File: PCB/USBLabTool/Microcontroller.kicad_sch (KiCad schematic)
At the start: 18 parts, among them J1 Conn_01x06_Pin, J18 02x02, J21 Conn_01x20_Pin, SW2 PTH_RA_h7.5mm, U12 STM32H562VGTx, Y1 32.768kHz

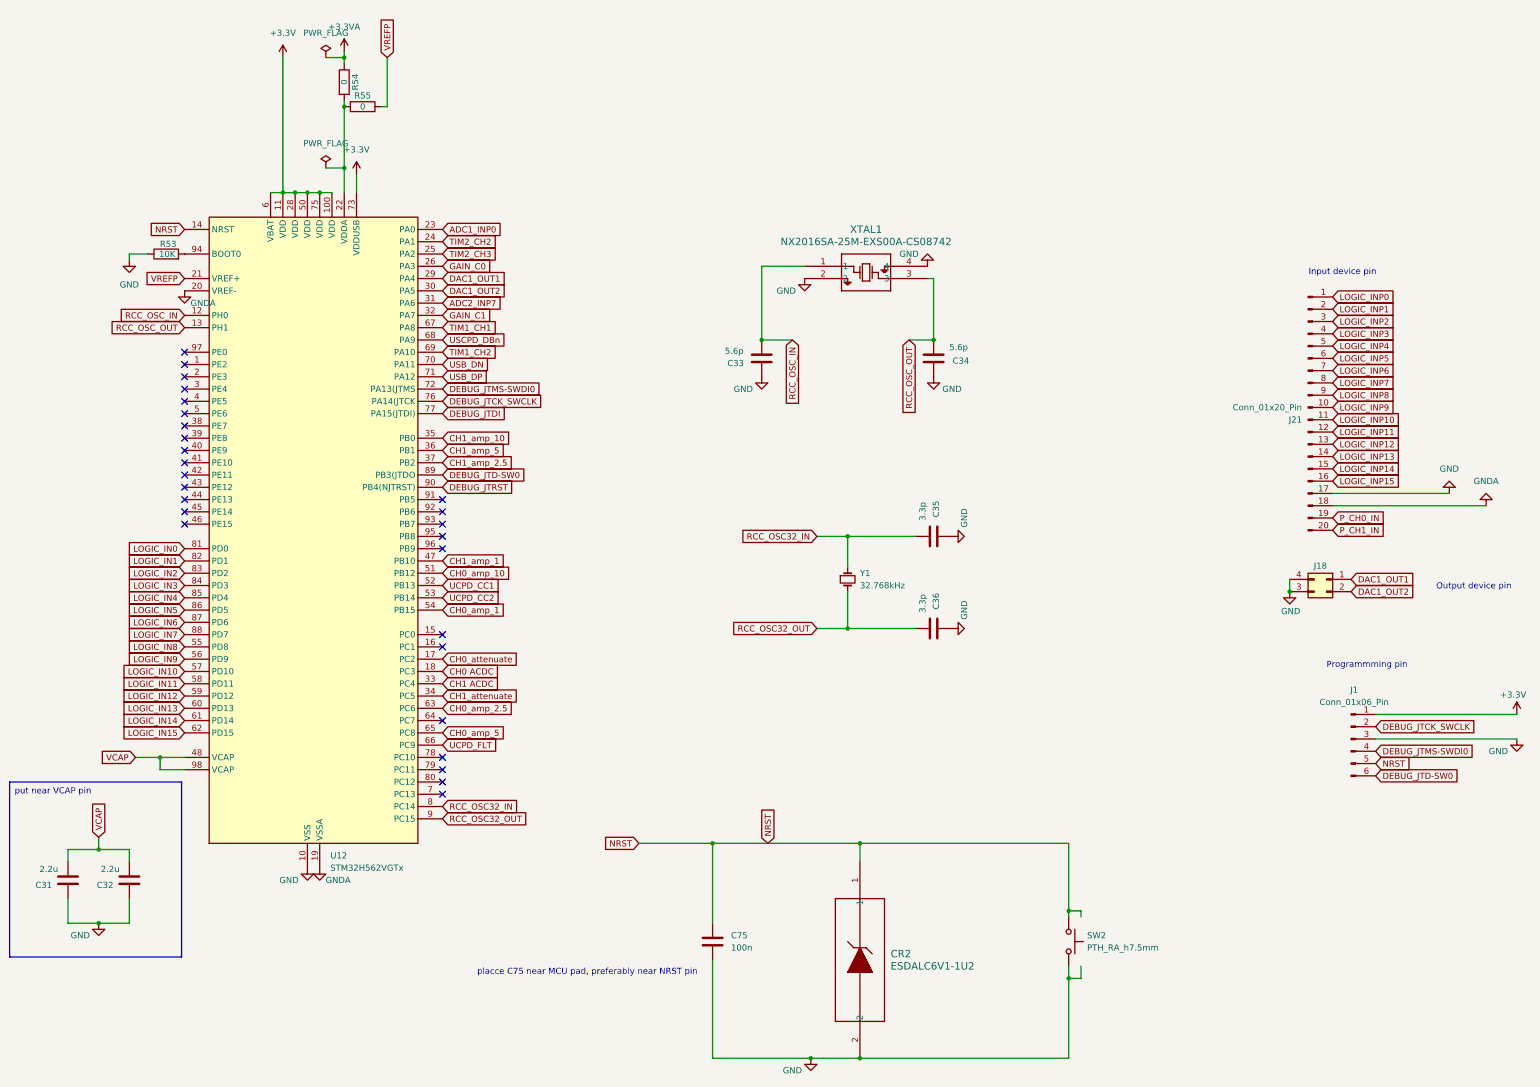
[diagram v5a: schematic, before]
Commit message: footprint with minor fixes
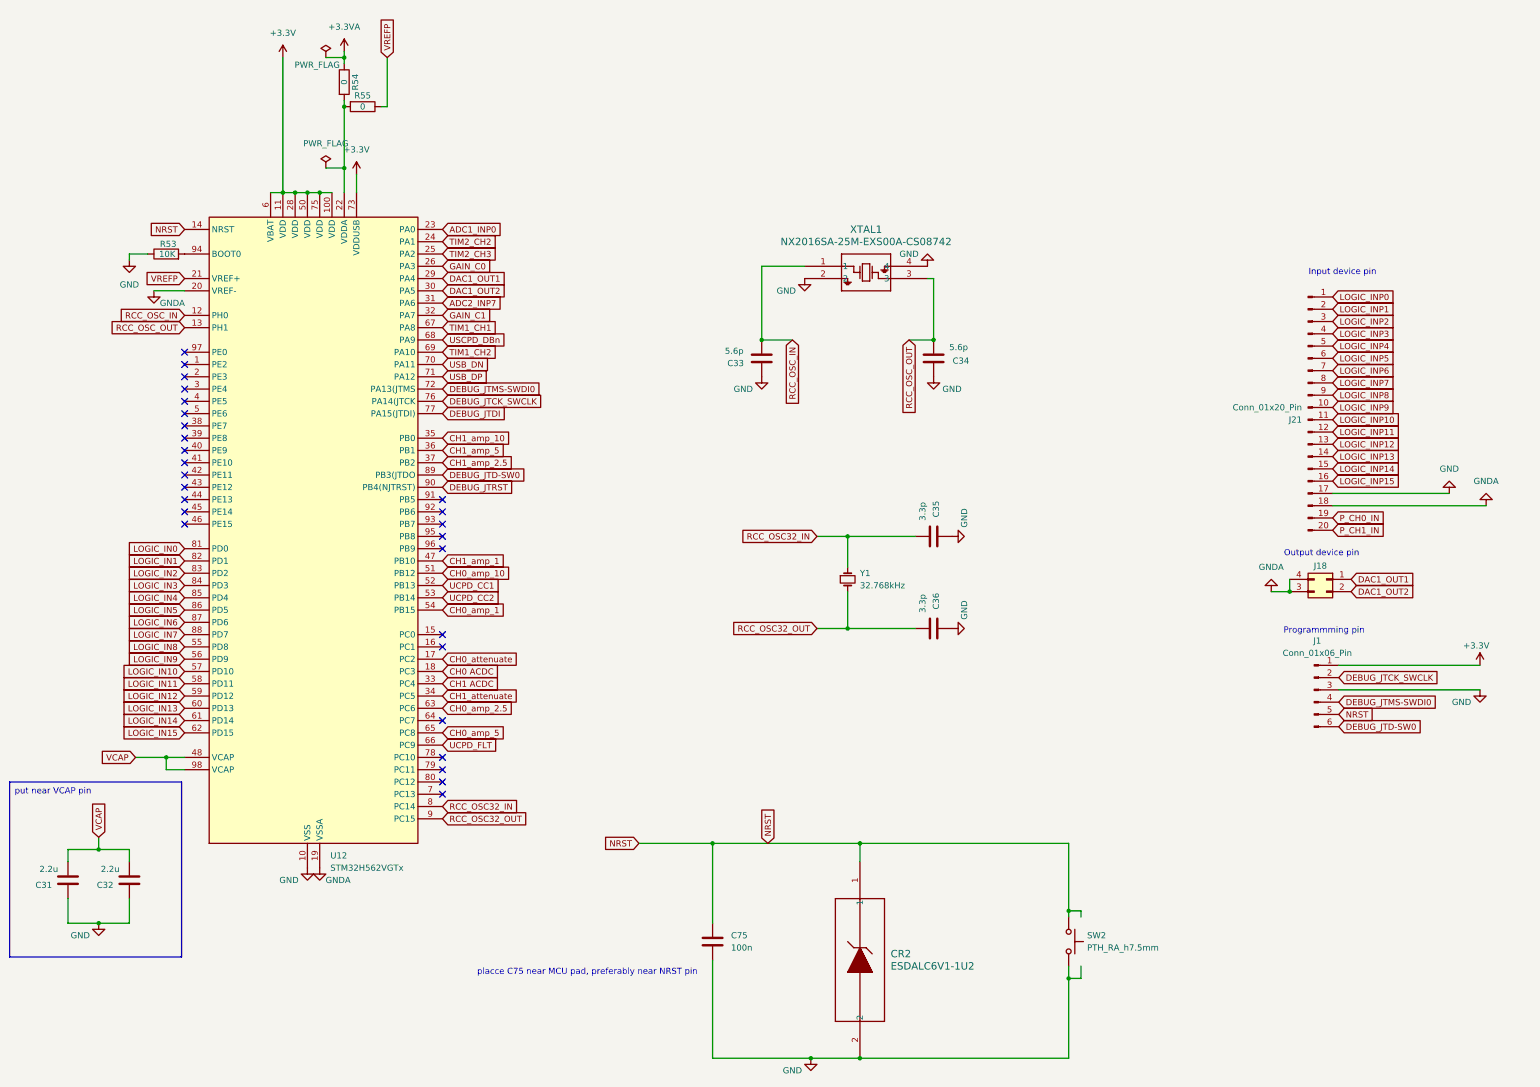
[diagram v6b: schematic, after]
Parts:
- J18: footprint awg_fp_lib:2x02 -> Connector_PinHeader_2.54mm:PinHeader_2x02_P2.54mm_Vertical
- SW2: footprint Button_Switch_THT:SW_PUSH_6mm_H7.3mm -> SparkFun-Switch:Push_SMD_6.2x6.2mm
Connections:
- net GND: no longer J18.3 (Pin_3), J18.4 (Pin_4)
- net GNDA: now also J18.3 (Pin_3), J18.4 (Pin_4)
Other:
- moved on the sheet: J1

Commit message: rearrange logic pins, connectors, fix some name tags
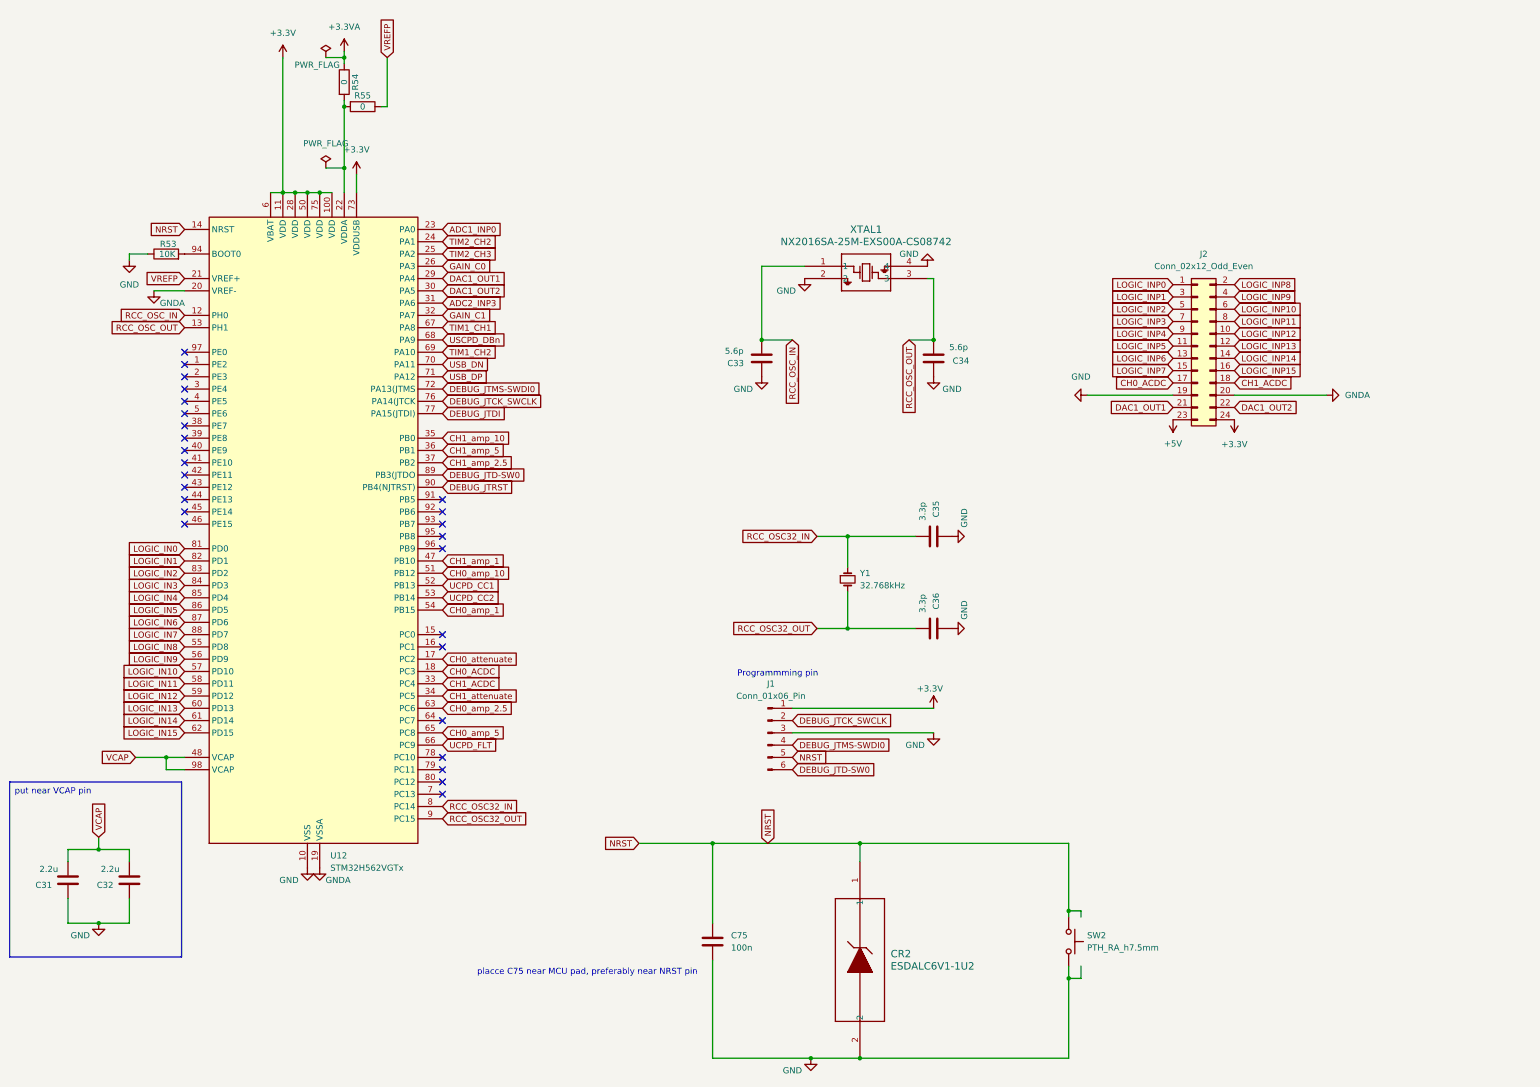
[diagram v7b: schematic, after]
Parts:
- removed J18: 02x02, Connector_PinHeader_2.54mm:PinHeader_2x02_P2.54mm_Vertical, symbol Connector_Generic:Conn_02x02_Counter_Clockwise
- removed J21: Conn_01x20_Pin, Connector_PinHeader_2.54mm:PinHeader_1x20_P2.54mm_Vertical, symbol Connector:Conn_01x20_Pin
- added J2: Conn_02x12_Odd_Even, Connector_JST:JST_PHD_S24B-PHDSS_2x12_P2.00mm_Horizontal, symbol Connector_Generic:Conn_02x12_Odd_Even
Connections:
- net +3.3V: now also J2.24 (Pin_24)
- net DAC1_OUT1: now also J2.21 (Pin_21)
- net DAC1_OUT2: now also J2.22 (Pin_22)
- net GND: now also J2.19 (Pin_19)
- net GNDA: now also J2.20 (Pin_20)
- net LOGIC_INP0: now also J2.1 (Pin_1)
- net LOGIC_INP1: now also J2.3 (Pin_3)
- net LOGIC_INP10: now also J2.6 (Pin_6)
- net LOGIC_INP11: now also J2.8 (Pin_8)
- net LOGIC_INP12: now also J2.10 (Pin_10)
- net LOGIC_INP13: now also J2.12 (Pin_12)
- net LOGIC_INP14: now also J2.14 (Pin_14)
- net LOGIC_INP15: now also J2.16 (Pin_16)
- net LOGIC_INP2: now also J2.5 (Pin_5)
- net LOGIC_INP3: now also J2.7 (Pin_7)
- net LOGIC_INP4: now also J2.9 (Pin_9)
- net LOGIC_INP5: now also J2.11 (Pin_11)
- net LOGIC_INP6: now also J2.13 (Pin_13)
- net LOGIC_INP7: now also J2.15 (Pin_15)
- net LOGIC_INP8: now also J2.2 (Pin_2)
- net LOGIC_INP9: now also J2.4 (Pin_4)
- net ADC2_INP7 renamed ADC2_INP3
- net CH0 ACDC renamed CH0_ACDC
- net CH0_ACDC: now also J2.17 (Pin_17)
- net CH1 ACDC renamed CH1_ACDC
- net CH1_ACDC: now also J2.18 (Pin_18)
- new net +5V: J2.23 (Pin_23)
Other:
- note removed: "Input device pin"
- note removed: "Output device pin"
- moved on the sheet: J1

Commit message: Updated schematic
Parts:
- removed SW2: PTH_RA_h7.5mm, SparkFun-Switch:Push_SMD_6.2x6.2mm, symbol SparkFun-Switch:SPST_Push_PTH_RA_h7.5mm
- added SW1: SW_Push, Button_Switch_THT:SW_PUSH_6mm_H7.3mm, symbol Switch:SW_Push
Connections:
- net GND: now also SW1.2
- net NRST: now also SW1.1
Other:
- moved on the sheet: C75, CR2
